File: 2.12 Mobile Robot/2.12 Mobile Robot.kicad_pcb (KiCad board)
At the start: 4 copper layers, 176 x 56 mm, 82 parts, among them J1 Motor Control R, J2 Motor Control L, J3 GND, J4 Motor Power R, J5 Battery Power, J6 Motor Power L, J7 3.3V, J8 UART, J9 5V, Q1 DMMT5401-7-F, Q2 DMG2305UX-13, SW1 SW_PWR, SW2 RST_SW, SW3 BOOT_SW, SW4 SW_PWR, U1 MOTOR_PWR, U2 ProS3, U3 TCA9548APWR, U4 POWER_IN, U5 TPS564208DDCT

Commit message: About to add JLCPCB libraries
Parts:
- removed E1: FL Encoder, Connector_JST:JST_PH_S4B-PH-SM4-TB_1x04-1MP_P2.00mm_Horizontal
- removed E2: BL Encoder, Connector_JST:JST_PH_S4B-PH-SM4-TB_1x04-1MP_P2.00mm_Horizontal
- removed E3: FR Encoder, Connector_JST:JST_PH_S4B-PH-SM4-TB_1x04-1MP_P2.00mm_Horizontal
- removed E4: BR Encoder, Connector_JST:JST_PH_S4B-PH-SM4-TB_1x04-1MP_P2.00mm_Horizontal
- added J10: FL Encoder, Connector_JST:JST_PH_S4B-PH-SM4-TB_1x04-1MP_P2.00mm_Horizontal, F.Cu at (100.4, 97.1)
- added J11: BL Encoder, Connector_JST:JST_PH_S4B-PH-SM4-TB_1x04-1MP_P2.00mm_Horizontal, F.Cu at (114.4, 97.1)
- added J12: FR Encoder, Connector_JST:JST_PH_S4B-PH-SM4-TB_1x04-1MP_P2.00mm_Horizontal, F.Cu at (128.5, 97.1)
- added J13: BR Encoder, Connector_JST:JST_PH_S4B-PH-SM4-TB_1x04-1MP_P2.00mm_Horizontal, F.Cu at (142.5, 97.1)
- D2: value PWR -> Power LED
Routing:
- net GND: track 137.1 -> 157.0 mm, vias 190 -> 276
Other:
- board text removed: "Back Left Enc"
- board text removed: "Back Right Enc"
- board text removed: "Front Left Enc"
- board text removed: "Front Right Enc"

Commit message: Tentatively ready for production
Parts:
- C1: footprint Capacitor_SMD:C_0805_2012Metric_Pad1.18x1.45mm_HandSolder -> footprint:0805_2012Metric
- C2: footprint Capacitor_SMD:C_1210_3225Metric -> footprint:0805_2012Metric
- D1, D2: footprint LED_SMD:LED_0603_1608Metric -> footprint:LED0603
- J5: footprint Connector_AMASS:AMASS_XT60PW-M_1x02_P7.20mm_Horizontal -> Connector_AMASS:AMASS_XT30PW-M_1x02_P2.50mm_Horizontal
- R1, R10, R11, R12, R13, R14, R15, R16, R17, R18, R19, R2, R20, R21, R22, R23, R24, R25, R26, R27, R28, R29, R3, R30, R31, R32, R33, R34, R4, R5, R6, R7, R8, R9: footprint Resistor_SMD:R_0603_1608Metric -> footprint:0603_1608Metric
- moved J5 5.37 mm to (175.4, 134.2)
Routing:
- net GND: vias 276 -> 291
- net /VBAT_IN: vias 34 -> 57
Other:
- board text added: "PWR LED"
- board text removed: "LED"

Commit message: Production files
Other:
- board text added: "- 6-13V +"
- board text removed: "+ 6-13V -"
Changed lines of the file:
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@@
     (property "ki_keywords" "DC power barrel jack connector")
     (attr through_hole)
-    (fp_text reference "J5" (at -2.5 -14.5 -90) (layer "F.SilkS")
+    (fp_text reference "J5" (at 5.54 -7.707) (layer "F.SilkS")
         (effects (font (size 1 1) (thickness 0.15)))
     )
@@
   (gr_arc (start 208 136) (mid 205.656854 141.656854) (end 200 144)
     (stroke (width 0.1) (type default)) (layer "Edge.Cuts"))
-  (gr_text " + 6-13V -" (at 193.294 143.256 90) (layer "F.SilkS")
+  (gr_text " - 6-13V +" (at 193.294 143.256 90) (layer "F.SilkS")
     (effects (font (size 2 2) (thickness 0.4) bold) (justify left bottom))
   )

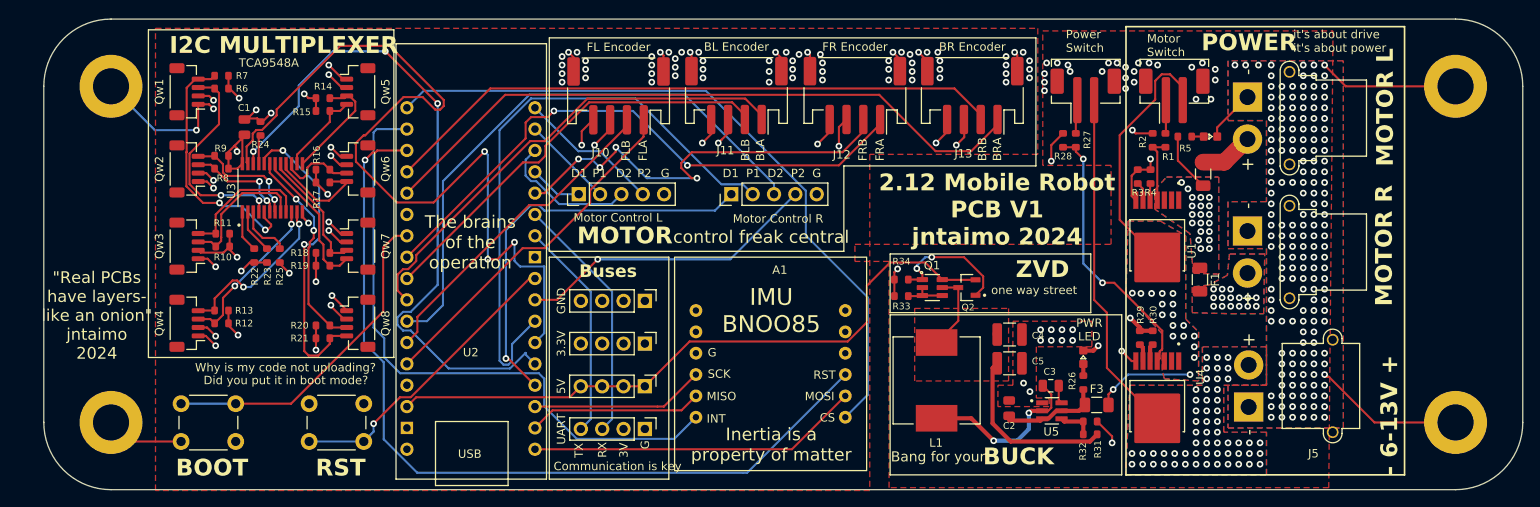
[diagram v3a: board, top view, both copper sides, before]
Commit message: Updated silkscreen to be generic
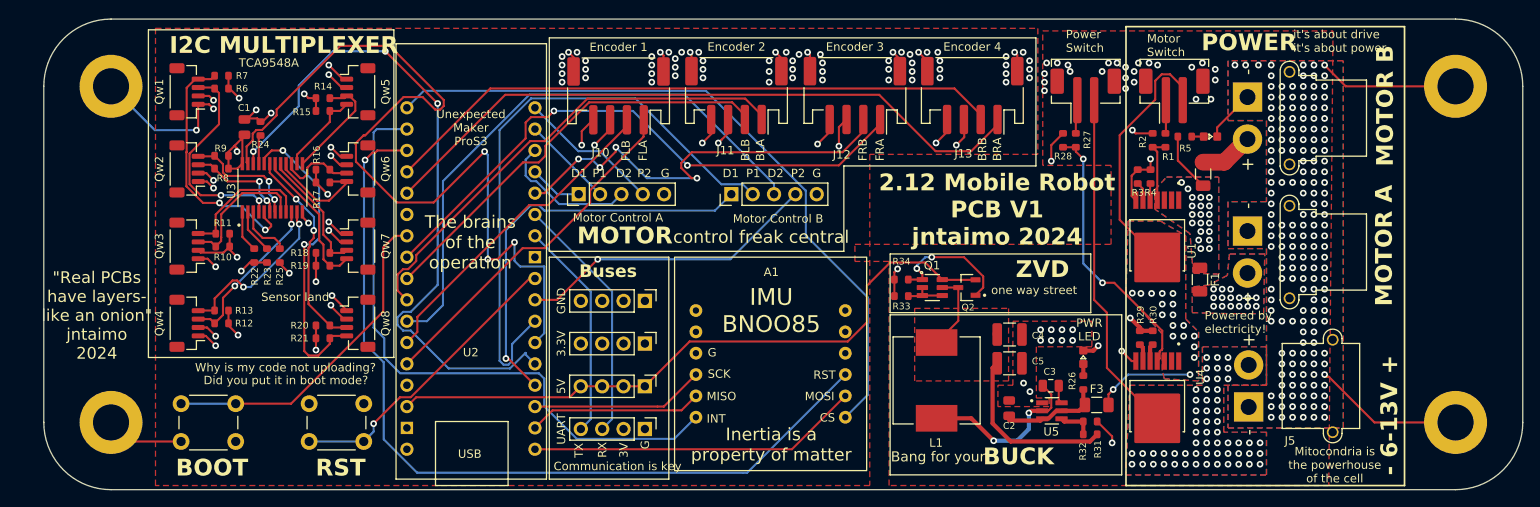
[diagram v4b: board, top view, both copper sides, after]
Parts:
- J1: value Motor Control R -> Motor Control B
- J10: value FL Encoder -> Encoder 1
- J11: value BL Encoder -> Encoder 2
- J12: value FR Encoder -> Encoder 3
- J13: value BR Encoder -> Encoder 4
- J2: value Motor Control L -> Motor Control A
- J4: value Motor Power R -> Motor Power A
- J6: value Motor Power L -> Motor Power B
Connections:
- net /DIR1_L renamed /DIR_1A
- net /DIR1_R renamed /DIR_1B
- net /DIR2_L renamed /DIR_2A
- net /DIR2_R renamed /DIR_2B
- net /HALL_BL_A renamed /HALL_2A
- net /HALL_BL_B renamed /HALL_2B
- net /HALL_BR_A renamed /HALL_4A
- net /HALL_BR_B renamed /HALL_4B
- net /HALL_FL_A renamed /HALL_1A
- net /HALL_FL_B renamed /HALL_1B
- net /HALL_FR_A renamed /HALL_3A
- net /HALL_FR_B renamed /HALL_3B
- net /L_MOTOR renamed /B_MOTOR
- net /PWM1_L renamed /PWM_1A
- net /PWM1_R renamed /PWM_1B
- net /PWM2_L renamed /PWM_2A
- net /PWM2_R renamed /PWM_2B
- net /R_MOTOR renamed /A_MOTOR
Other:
- board text added: "MOTOR A"
- board text added: "MOTOR B"
- board text added: "Mitocondria is the powerhouse of the cell"
- board text added: "Powered by electricity!"
- board text added: "Sensor land"
- board text added: "Unexpected Maker ProS3"
- board text removed: "MOTOR L"
- board text removed: "MOTOR R"
